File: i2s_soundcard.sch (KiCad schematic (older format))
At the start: 5 parts, among them J1 Conn_01x08, J2 Conn_01x06, U1 TLV320AIC3104IRHBT

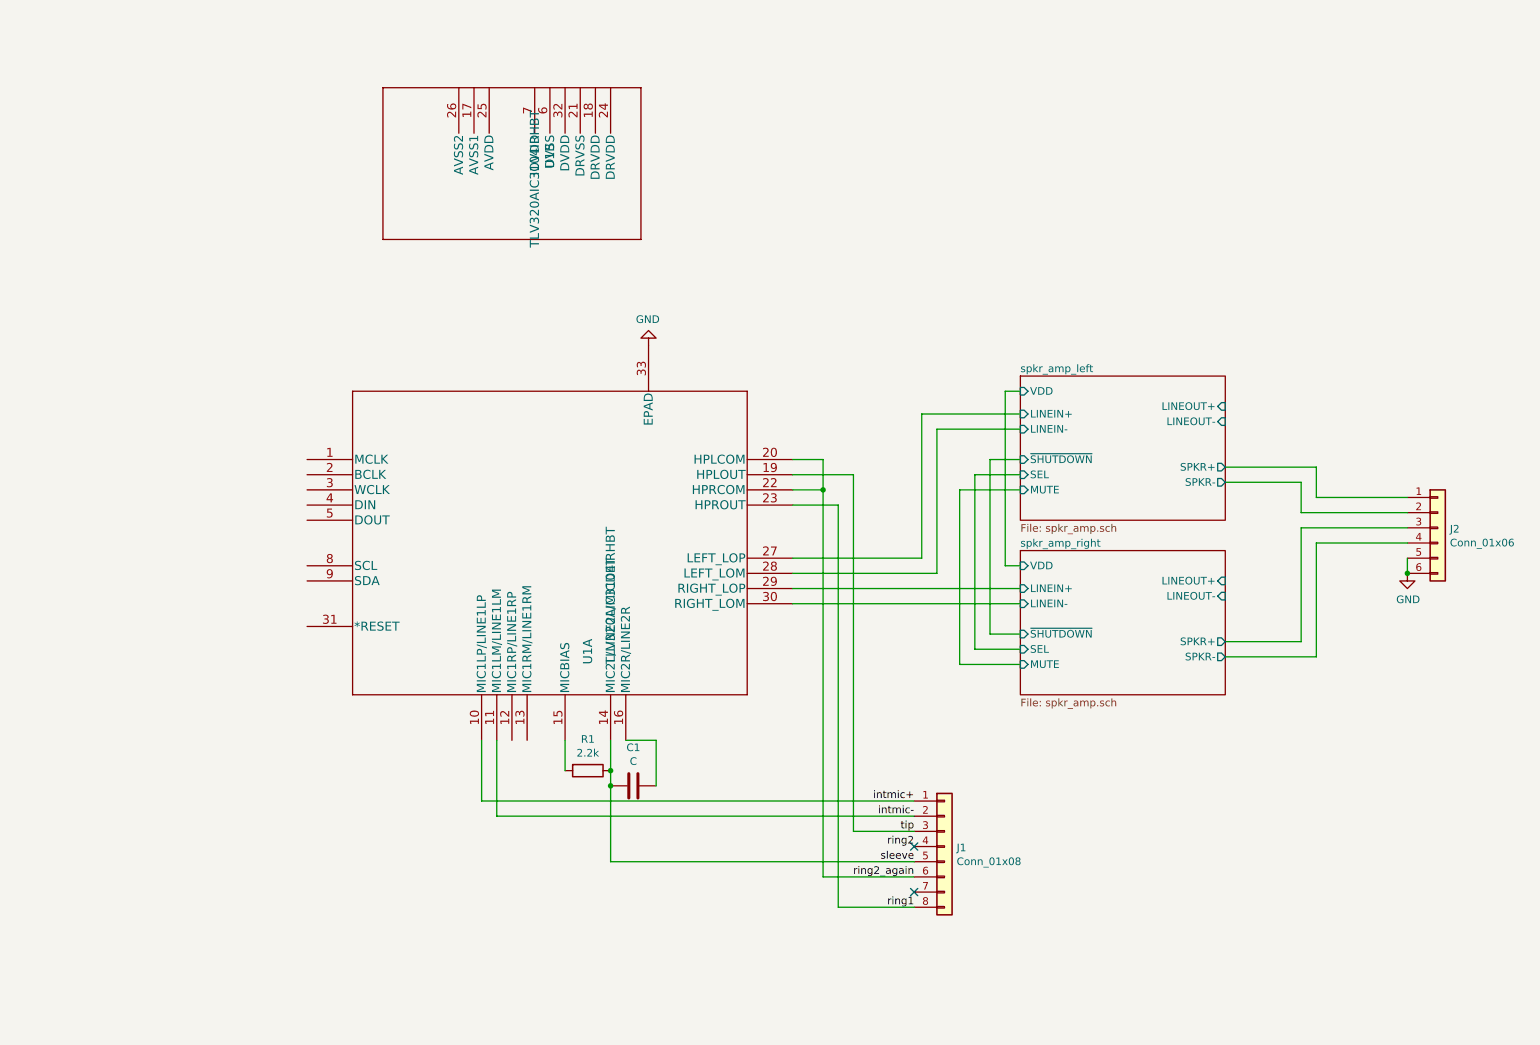
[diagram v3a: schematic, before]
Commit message: Lots more routing; set V pads on TPA2006 to GND; add 1.8V/3.3V dual LDO: TLV7111830. Save datasheets to project directory for safe keeping.
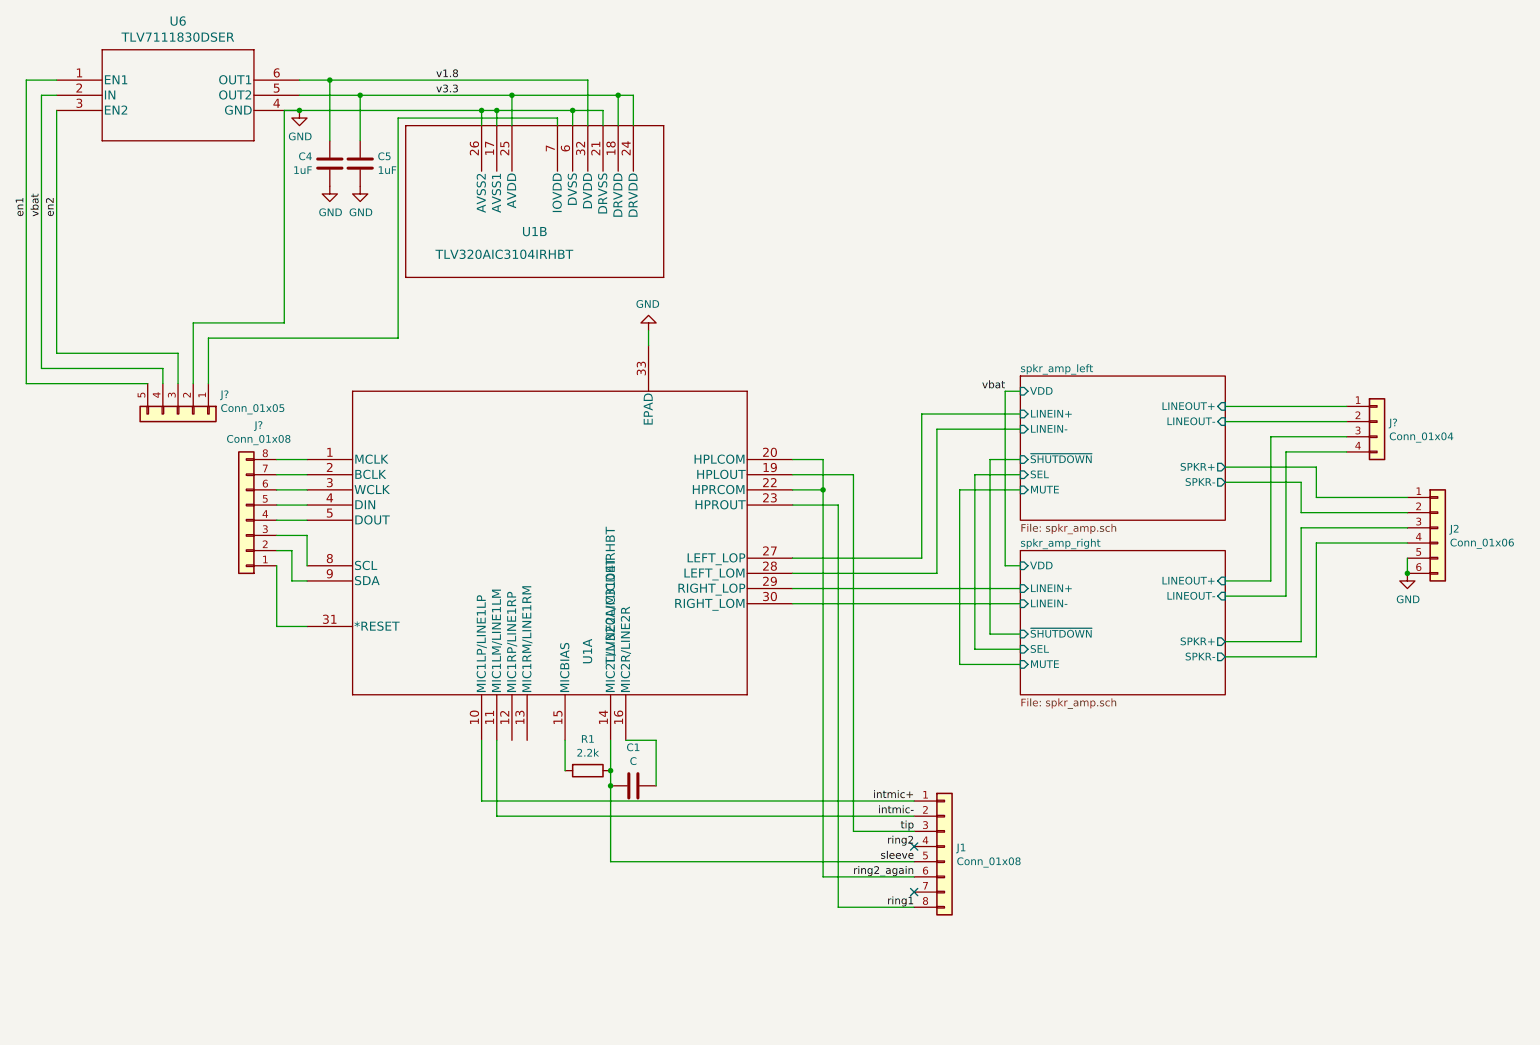
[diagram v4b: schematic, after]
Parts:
- added C4, C5: 1uF, Capacitor_SMD:C_0402_1005Metric, symbol Device:C
- added J?: Conn_01x08, symbol Connector_Generic:Conn_01x08
- added J?: Conn_01x04, symbol Connector_Generic:Conn_01x04
- added J?: Conn_01x05, symbol Connector_Generic:Conn_01x05
- added U6: TLV7111830DSER, footprints:TLV7111830DSER, symbol TLV7111830DSER:TLV7111830DSER
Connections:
- net GND: now also U1.17 (AVSS1), U1.21 (DRVSS), U1.26 (AVSS2), U1.6 (DVSS), C4.1, C5.2, J?.2 (Pin_2), U6.4 (GND)
- net spkr_amp_left/LINEOUT+: now also J?.1 (Pin_1)
- net spkr_amp_left/LINEOUT-: now also J?.2 (Pin_2)
- net spkr_amp_right/LINEOUT+: now also J?.3 (Pin_3)
- net spkr_amp_right/LINEOUT-: now also J?.4 (Pin_4)
- net v3.3: now reaches U1.18 (DRVDD)
- net v3.3: now also U1.24 (DRVDD), U1.25 (AVDD), C5.1, U6.5 (OUT2)
- net v1.8: now reaches U1.32 (DVDD)
- net v1.8: now also C4.2, U6.6 (OUT1)
- net at U1.7 (IOVDD): now also J?.1 (Pin_1)
- net at U1.1 (MCLK): now also J?.8 (Pin_8)
- net at U1.2 (BCLK): now also J?.7 (Pin_7)
- net at U1.3 (WCLK): now also J?.6 (Pin_6)
- net at U1.31 (*RESET): now also J?.1 (Pin_1)
- net at U1.4 (DIN): now also J?.5 (Pin_5)
- net at U1.5 (DOUT): now also J?.4 (Pin_4)
- net at U1.8 (SCL): now also J?.3 (Pin_3)
- net at U1.9 (SDA): now also J?.2 (Pin_2)
- new net en1: J?.5 (Pin_5), U6.1 (EN1)
- new net en2: J?.3 (Pin_3), U6.3 (EN2)
- new net vbat: J?.4 (Pin_4), U6.2 (IN)
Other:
- moved on the sheet: U1B

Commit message: Break out more nets to pins, move switches down to make room for those traces. Reroute a lot of things.
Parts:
- J3: renamed from J?; footprint (none) -> Connector_PinHeader_1.00mm:PinHeader_1x05_P1.00mm_Vertical
- J4: renamed from J?; value Conn_01x08 -> Conn_01x11; footprint (none) -> Connector_PinHeader_1.00mm:PinHeader_1x11_P1.00mm_Vertical; symbol Connector_Generic:Conn_01x08 -> Connector_Generic:Conn_01x11
- J5: renamed from J?; footprint (none) -> Connector_PinHeader_1.00mm:PinHeader_1x04_P1.00mm_Vertical
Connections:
- net iovdd: now reaches J3.1 (Pin_1), U1.7 (IOVDD)
- net mclk: now reaches U1.1 (MCLK)
- net mclk: now also J4.7 (Pin_7); no longer J4.8 (Pin_8)
- net bclk: now reaches U1.2 (BCLK)
- net bclk: now also J4.6 (Pin_6); no longer J4.7 (Pin_7)
- net wclk: now reaches U1.3 (WCLK)
- net wclk: now also J4.5 (Pin_5); no longer J4.6 (Pin_6)
- net reset: now reaches U1.31 (*RESET)
- net reset: now also J4.8 (Pin_8); no longer J4.1 (Pin_1)
- net din: now reaches U1.4 (DIN)
- net din: now also J4.4 (Pin_4); no longer J4.5 (Pin_5)
- net dout: now reaches U1.5 (DOUT)
- net dout: now also J4.3 (Pin_3); no longer J4.4 (Pin_4)
- net scl: now reaches U1.8 (SCL)
- net scl: now also J4.2 (Pin_2); no longer J4.3 (Pin_3)
- net sca: now reaches U1.9 (SDA)
- net sca: now also J4.1 (Pin_1); no longer J4.2 (Pin_2)
- net spkr_amp_left/LINEOUT+ renamed LOR+
- net spkr_amp_left/LINEOUT- renamed LOR-
- net spkr_amp_right/LINEOUT+ renamed LOL+
- net spkr_amp_right/LINEOUT- renamed LOL-
- new net mute: J4.9 (Pin_9)
- new net sel: J4.10 (Pin_10)
- new net ~shutdown: J4.11 (Pin_11)
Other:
- moved on the sheet: J3
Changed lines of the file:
@@
 	1200 950  1200 2550
 Wire Wire Line
-	1200 2550 2000 2550
-Wire Wire Line
-	2000 2550 2000 2750
-Wire Wire Line
-	1900 2750 1900 2650
-Wire Wire Line
-	1900 2650 1100 2650
+	1200 2550 1550 2550
+Wire Wire Line
+	1550 2550 1550 2750
+Wire Wire Line
+	1450 2750 1450 2650
+Wire Wire Line
+	1450 2650 1100 2650
 Wire Wire Line
 	1100 2650 1100 850
@@
 	1100 850  1200 850
 Wire Wire Line
-	1800 2750 1000 2750
+	1350 2750 1000 2750
 Wire Wire Line
 	1000 2750 1000 750
@@
 Wire Wire Line
 	3450 1000 3450 2450
-Wire Wire Line
-	3450 2450 2200 2450
-Wire Wire Line
-	2200 2450 2200 2750
 $Comp
 L Device:C C4
@@
 vbat
 $Comp
-L Connector_Generic:Conn_01x08 J?
+L Connector_Generic:Conn_01x11 J4
 U 1 1 6035D713
-P 2450 3650
-F 0 "J?" H 2368 3025 50  0000 C CNN
-F 1 "Conn_01x08" H 2368 3116 50  0000 C CNN
-F 2 "" H 2450 3650 50  0001 C CNN
-F 3 "~" H 2450 3650 50  0001 C CNN
-	1    2450 3650
+P 2250 3350
+F 0 "J4" H 2168 2625 50  0000 C CNN
+F 1 "Conn_01x11" H 1850 2700 50  0000 C CNN
+F 2 "Connector_PinHeader_1.00mm:PinHeader_1x11_P1.00mm_Vertical" H 2250 3350 50  0001 C CNN
+F 3 "~" H 2250 3350 50  0001 C CNN
+	1    2250 3350
 	-1   0    0    1
 $EndComp
@@
 $EndComp
 Wire Wire Line
-	2850 3250 2650 3250
-Wire Wire Line
-	2850 3350 2650 3350
-Wire Wire Line
-	2850 3450 2650 3450
-Wire Wire Line
-	2850 3550 2650 3550
-Wire Wire Line
-	2850 3650 2650 3650
-Wire Wire Line
 	2850 3950 2850 3750
 Wire Wire Line
-	2850 3750 2650 3750
-Wire Wire Line
 	2850 4050 2750 4050
 Wire Wire Line
 	2750 4050 2750 3850
-Wire Wire Line
-	2750 3850 2650 3850
-Wire Wire Line
-	2850 4350 2650 4350
-Wire Wire Line
-	2650 4350 2650 3950
-$Comp
-L Connector_Generic:Conn_01x04 J?
+$Comp
+L Connector_Generic:Conn_01x04 J5
 U 1 1 6037CBEB
 P 9900 3000
-F 0 "J?" H 9980 2992 50  0000 L CNN
+F 0 "J5" H 9980 2992 50  0000 L CNN
 F 1 "Conn_01x04" H 9980 2901 50  0000 L CNN
-F 2 "" H 9900 3000 50  0001 C CNN
+F 2 "Connector_PinHeader_1.00mm:PinHeader_1x04_P1.00mm_Vertical" H 9900 3000 50  0001 C CNN
 F 3 "~" H 9900 3000 50  0001 C CNN
 	1    9900 3000
@@
 	2700 950  2700 2350
 Wire Wire Line
-	2700 2350 2100 2350
-Wire Wire Line
-	2100 2350 2100 2750
-$Comp
-L Connector_Generic:Conn_01x05 J?
+	2700 2350 1650 2350
+Wire Wire Line
+	1650 2350 1650 2750
+$Comp
+L Connector_Generic:Conn_01x05 J3
 U 1 1 60399FB4
-P 2000 2950
-F 0 "J?" V 1872 3230 50  0000 L CNN
-F 1 "Conn_01x05" V 1963 3230 50  0000 L CNN
-F 2 "" H 2000 2950 50  0001 C CNN
-F 3 "~" H 2000 2950 50  0001 C CNN
-	1    2000 2950
+P 1550 2950
+F 0 "J3" V 1550 2550 50  0000 L CNN
+F 1 "Conn_01x05" V 1650 2600 50  0000 L CNN
+F 2 "Connector_PinHeader_1.00mm:PinHeader_1x05_P1.00mm_Vertical" H 1550 2950 50  0001 C CNN
+F 3 "~" H 1550 2950 50  0001 C CNN
+	1    1550 2950
 	0    1    1    0
 $EndComp
+Text Label 2650 3250 0    50   ~ 0
+mclk
+Text Label 2650 3350 0    50   ~ 0
+bclk
+Text Label 2650 3450 0    50   ~ 0
+wclk
+Text Label 2650 3550 0    50   ~ 0
+din
+Text Label 2650 3650 0    50   ~ 0
+dout
+Text Label 2650 3750 0    50   ~ 0
+scl
+Text Label 2650 3850 0    50   ~ 0
+sca
+Text Label 1800 2450 0    50   ~ 0
+iovdd
+Text Label 9400 2900 0    50   ~ 0
+LOR+
+Text Label 9400 3000 0    50   ~ 0
+LOR-
+Text Label 9400 3200 0    50   ~ 0
+LOL-
+Text Label 9400 3100 0    50   ~ 0
+LOL+
+Text Label 7350 4400 1    50   ~ 0
+~shutdown
+Text Label 7250 4500 1    50   ~ 0
+sel
+Text Label 7150 4600 1    50   ~ 0
+mute
+Text Label 2450 3050 0    50   ~ 0
+mute
+Text Label 2450 2950 0    50   ~ 0
+sel
+Text Label 2450 2850 0    50   ~ 0
+~shutdown
+Text Label 2650 3150 0    50   ~ 0
+reset
+Wire Wire Line
+	2450 3850 2750 3850
+Wire Wire Line
+	2450 3750 2850 3750
+Wire Wire Line
+	2450 3650 2850 3650
+Wire Wire Line
+	2450 3550 2850 3550
+Wire Wire Line
+	2450 3450 2850 3450
+Wire Wire Line
+	2450 3350 2850 3350
+Wire Wire Line
+	2450 3250 2850 3250
+Wire Wire Line
+	2850 4350 2600 4350
+Wire Wire Line
+	2600 4350 2600 3150
+Wire Wire Line
+	2600 3150 2450 3150
+Wire Wire Line
+	2650 3150 2600 3150
+Connection ~ 2600 3150
+Wire Wire Line
+	1750 2750 1750 2450
+Wire Wire Line
+	1750 2450 3450 2450
 $EndSCHEMATC

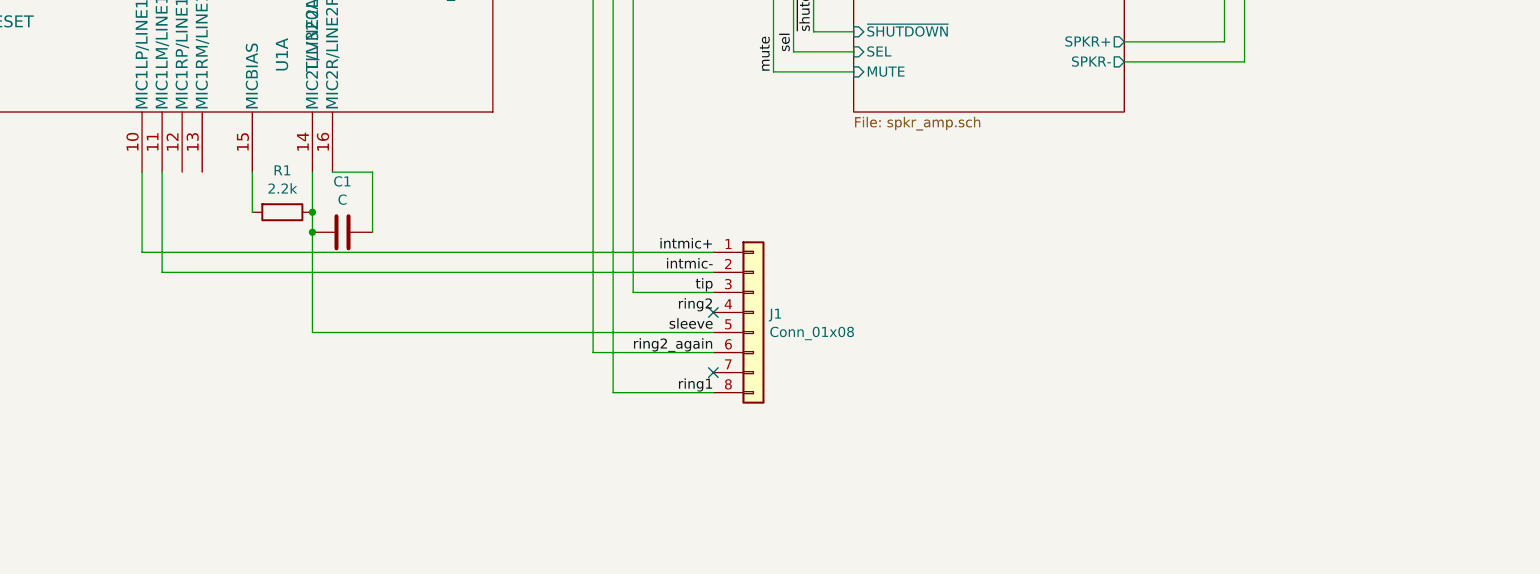
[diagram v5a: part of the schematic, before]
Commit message: Add TVS diodes on all the headphone port pins
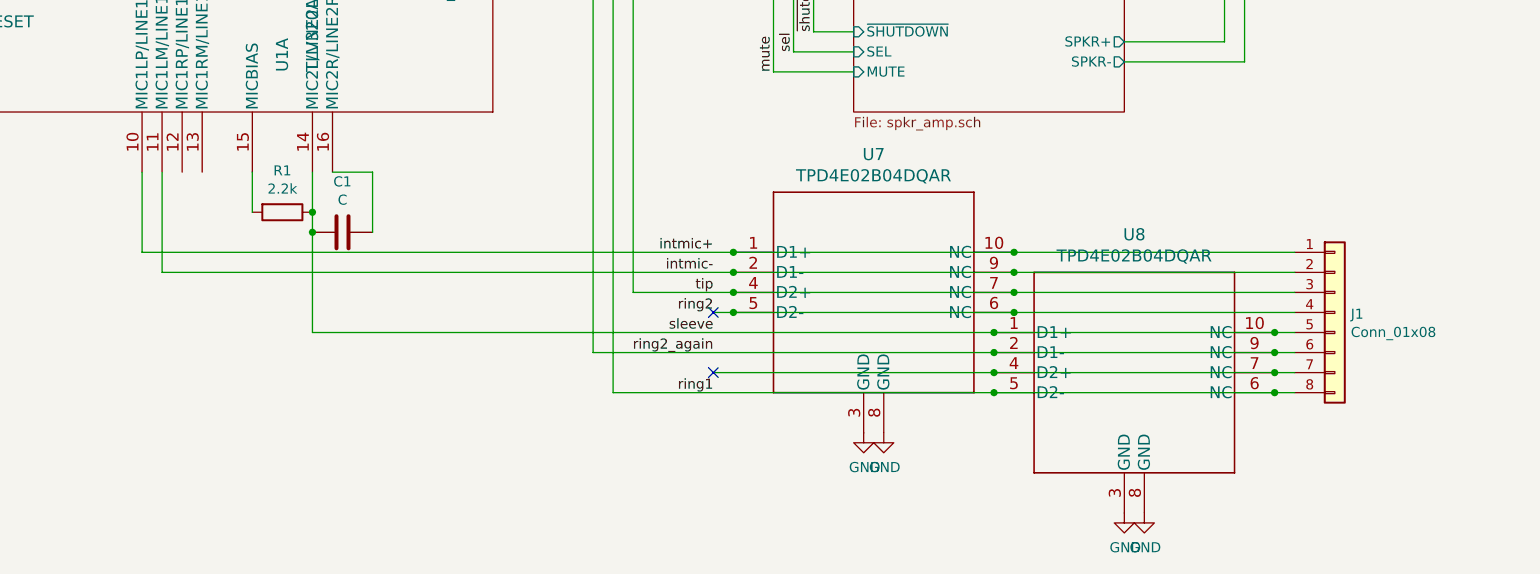
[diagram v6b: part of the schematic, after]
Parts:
- added U7, U8: TPD4E02B04DQAR, footprints:TPD4E02B04DQAR, symbol TPD4E02B04DQAR:TPD4E02B04DQAR
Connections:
- net GND: now also U7.3 (GND), U7.8 (GND), U8.3 (GND), U8.8 (GND)
- net intmic+: now also U7.1 (D1+), U7.10 (NC)
- net intmic-: now also U7.2 (D1-), U7.9 (NC)
- net ring1: now also U8.5 (D2-), U8.6 (NC)
- net ring2: now also U7.5 (D2-), U7.6 (NC)
- net ring2_again: now also U8.2 (D1-), U8.9 (NC)
- net sleeve: now also U8.1 (D1+), U8.10 (NC)
- net tip: now also U7.4 (D2+), U7.7 (NC)
- net at J1.7 (Pin_7): now also U8.4 (D2+), U8.7 (NC)
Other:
- moved on the sheet: J1
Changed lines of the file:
@@
 L Connector_Generic:Conn_01x08 J1
 U 1 1 60262BE3
-P 7050 5800
-F 0 "J1" H 7130 5792 50  0000 L CNN
-F 1 "Conn_01x08" H 7130 5701 50  0000 L CNN
-F 2 "footprints:FF18-8A-R11AD-B-3H" H 7050 5800 50  0001 C CNN
-F 3 "~" H 7050 5800 50  0001 C CNN
-	1    7050 5800
+P 9950 5800
+F 0 "J1" H 10030 5792 50  0000 L CNN
+F 1 "Conn_01x08" H 10030 5701 50  0000 L CNN
+F 2 "footprints:FF18-8A-R11AD-B-3H" H 9950 5800 50  0001 C CNN
+F 3 "~" H 9950 5800 50  0001 C CNN
+	1    9950 5800
 	1    0    0    -1
 $EndComp
@@
 	4100 5600 4100 5100
 Wire Wire Line
-	4000 5500 6850 5500
-Wire Wire Line
-	4100 5600 6850 5600
-Wire Wire Line
-	6850 5700 6450 5700
-Wire Wire Line
 	6450 5700 6450 3350
 Wire Wire Line
@@
 Wire Wire Line
 	6350 3550 6350 6200
-Wire Wire Line
-	6350 6200 6850 6200
-Wire Wire Line
-	6850 6000 6250 6000
 Wire Wire Line
 	6250 6000 6250 3450
@@
 Wire Wire Line
 	4550 5300 4550 5100
-Wire Wire Line
-	4850 5900 6850 5900
 Wire Wire Line
 	4850 5400 4850 5900
@@
 Wire Wire Line
 	1750 2450 3450 2450
+$Comp
+L TPD4E02B04DQAR:TPD4E02B04DQAR U7
+U 1 1 604B74AB
+P 7650 5700
+F 0 "U7" H 7650 6388 60  0000 C CNN
+F 1 "TPD4E02B04DQAR" H 7650 6282 60  0000 C CNN
+F 2 "footprints:TPD4E02B04DQAR" H 7650 5640 60  0001 C CNN
+F 3 "" H 7650 5700 60  0000 C CNN
+	1    7650 5700
+	1    0    0    -1
+$EndComp
+$Comp
+L TPD4E02B04DQAR:TPD4E02B04DQAR U8
+U 1 1 6053770A
+P 8950 6100
+F 0 "U8" H 8950 6788 60  0000 C CNN
+F 1 "TPD4E02B04DQAR" H 8950 6682 60  0000 C CNN
+F 2 "footprints:TPD4E02B04DQAR" H 8950 6040 60  0001 C CNN
+F 3 "" H 8950 6100 60  0000 C CNN
+	1    8950 6100
+	1    0    0    -1
+$EndComp
+Wire Wire Line
+	4000 5500 6950 5500
+Wire Wire Line
+	4100 5600 6950 5600
+Wire Wire Line
+	6450 5700 6950 5700
+Wire Wire Line
+	6850 5800 6950 5800
+Wire Wire Line
+	4850 5900 8250 5900
+Wire Wire Line
+	6250 6000 8250 6000
+Wire Wire Line
+	9750 6100 9650 6100
+Wire Wire Line
+	6350 6200 8250 6200
+Wire Wire Line
+	8350 5500 9750 5500
+Wire Wire Line
+	8350 5800 9750 5800
+Wire Wire Line
+	8350 5600 9750 5600
+Wire Wire Line
+	8350 5700 9750 5700
+Wire Wire Line
+	9650 5900 9750 5900
+Wire Wire Line
+	9650 6200 9750 6200
+Wire Wire Line
+	9650 6000 9750 6000
+Wire Wire Line
+	8250 6100 6850 6100
+$Comp
+L power:GND #PWR0106
+U 1 1 6055AD56
+P 8900 6800
+F 0 "#PWR0106" H 8900 6550 50  0001 C CNN
+F 1 "GND" H 8905 6627 50  0000 C CNN
+F 2 "" H 8900 6800 50  0001 C CNN
+F 3 "" H 8900 6800 50  0001 C CNN
+	1    8900 6800
+	1    0    0    -1
+$EndComp
+$Comp
+L power:GND #PWR0107
+U 1 1 6055B087
+P 9000 6800
+F 0 "#PWR0107" H 9000 6550 50  0001 C CNN
+F 1 "GND" H 9005 6627 50  0000 C CNN
+F 2 "" H 9000 6800 50  0001 C CNN
+F 3 "" H 9000 6800 50  0001 C CNN
+	1    9000 6800
+	1    0    0    -1
+$EndComp
+$Comp
+L power:GND #PWR0108
+U 1 1 6055B29C
+P 7700 6400
+F 0 "#PWR0108" H 7700 6150 50  0001 C CNN
+F 1 "GND" H 7705 6227 50  0000 C CNN
+F 2 "" H 7700 6400 50  0001 C CNN
+F 3 "" H 7700 6400 50  0001 C CNN
+	1    7700 6400
+	1    0    0    -1
+$EndComp
+$Comp
+L power:GND #PWR0109
+U 1 1 6055B7F2
+P 7600 6400
+F 0 "#PWR0109" H 7600 6150 50  0001 C CNN
+F 1 "GND" H 7605 6227 50  0000 C CNN
+F 2 "" H 7600 6400 50  0001 C CNN
+F 3 "" H 7600 6400 50  0001 C CNN
+	1    7600 6400
+	1    0    0    -1
+$EndComp
+Wire Wire Line
+	8250 5900 9650 5900
+Connection ~ 8250 5900
+Connection ~ 9650 5900
+Wire Wire Line
+	9650 6000 8250 6000
+Connection ~ 9650 6000
+Connection ~ 8250 6000
+Wire Wire Line
+	8250 6100 9650 6100
+Connection ~ 8250 6100
+Connection ~ 9650 6100
+Wire Wire Line
+	9650 6200 8250 6200
+Connection ~ 9650 6200
+Connection ~ 8250 6200
+Wire Wire Line
+	8350 5800 6950 5800
+Connection ~ 8350 5800
+Connection ~ 6950 5800
+Wire Wire Line
+	6950 5700 8350 5700
+Connection ~ 6950 5700
+Connection ~ 8350 5700
+Wire Wire Line
+	8350 5600 6950 5600
+Connection ~ 8350 5600
+Connection ~ 6950 5600
+Wire Wire Line
+	6950 5500 8350 5500
+Connection ~ 6950 5500
+Connection ~ 8350 5500
 $EndSCHEMATC
